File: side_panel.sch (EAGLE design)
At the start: 47 parts

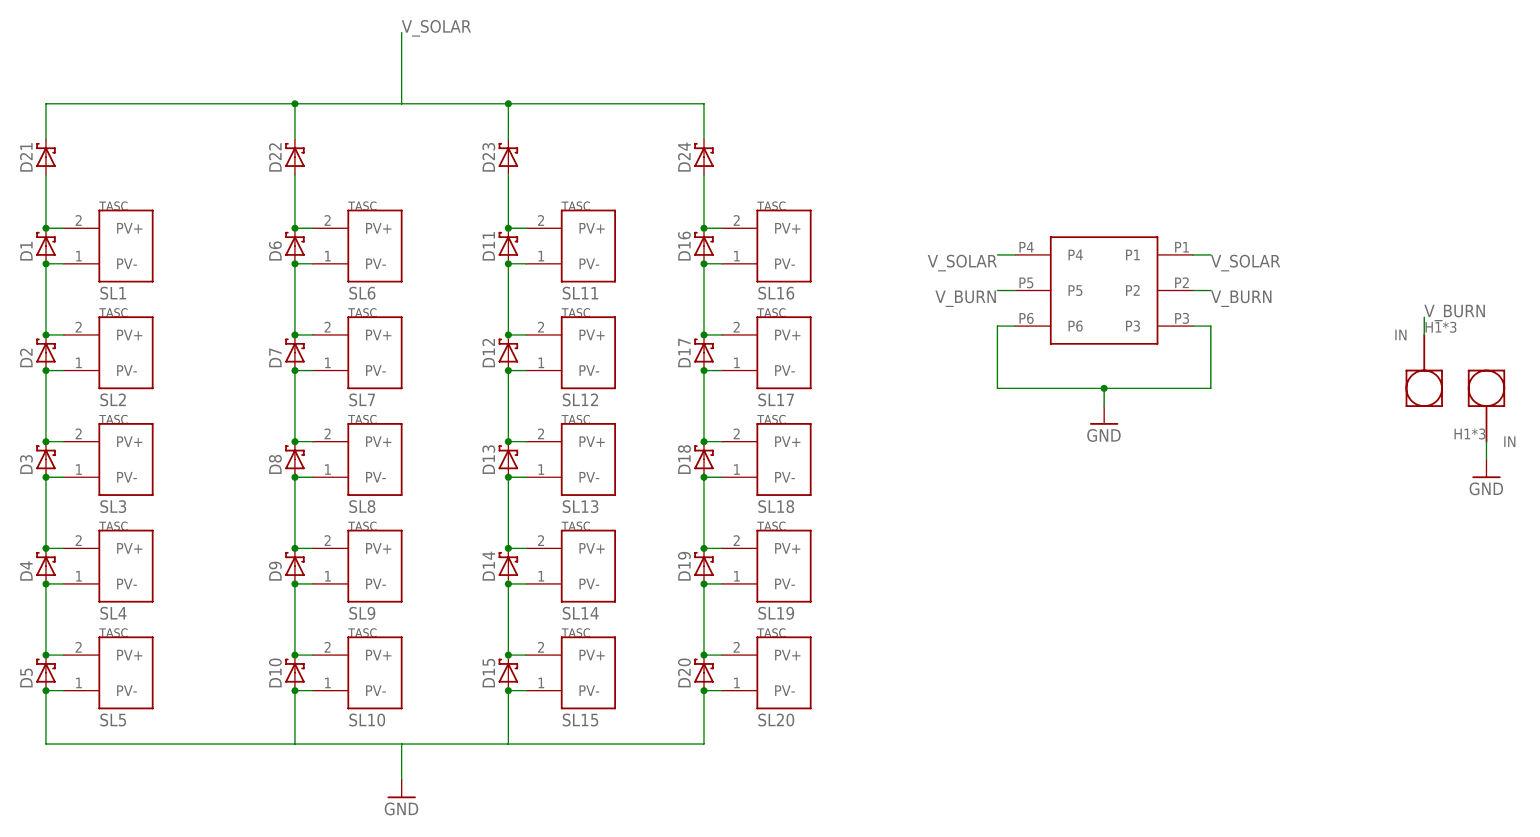
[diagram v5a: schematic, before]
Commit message: Beginning of new solar panel layout
Changing to pairs of TASC cells to accommodate irregularities in
dimensions
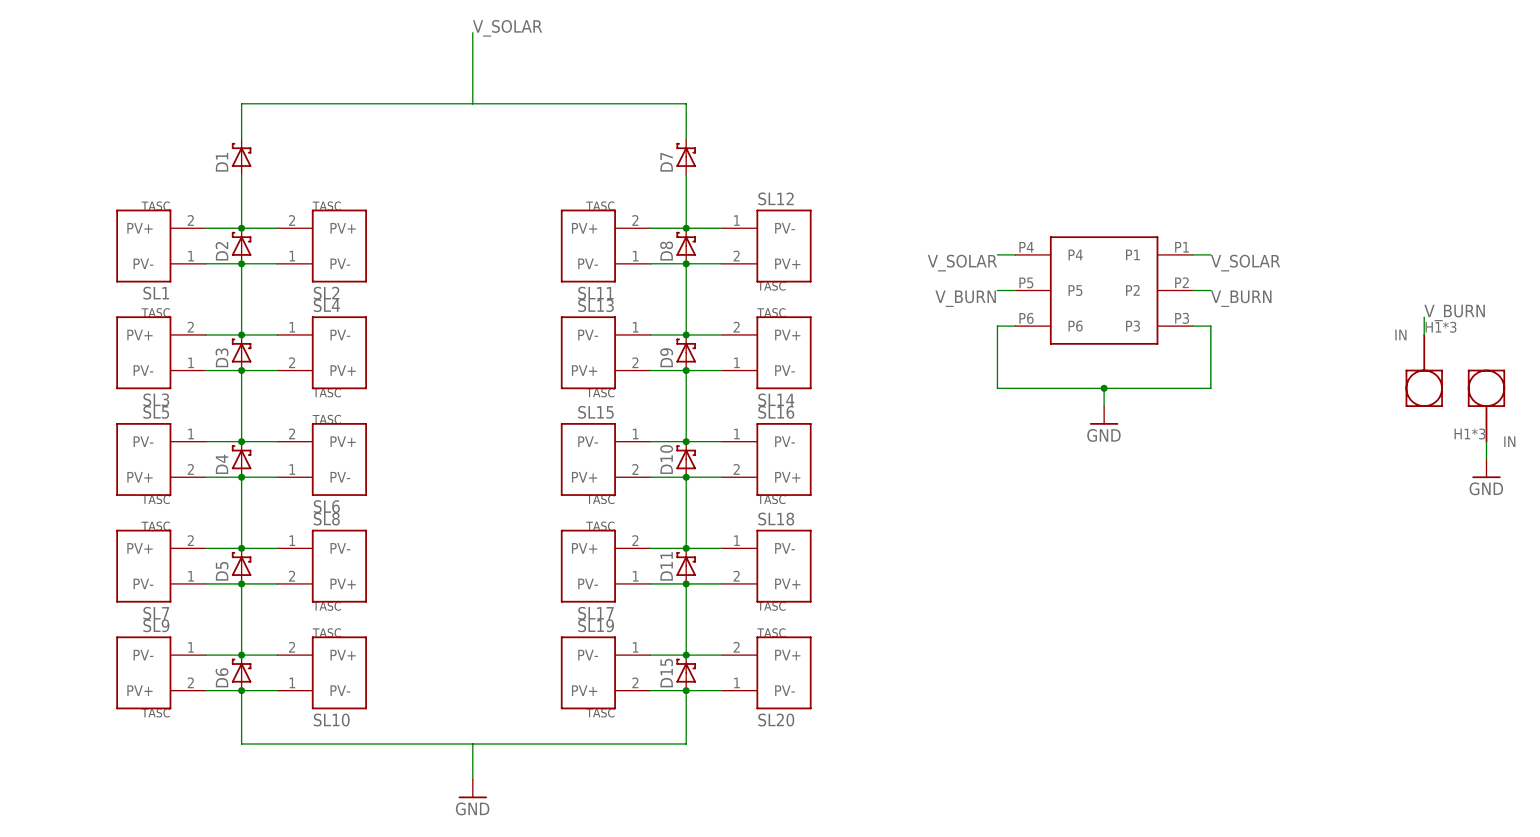
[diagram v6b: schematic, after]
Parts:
- removed D12, D13, D14, D16, D17, D18, D19, D20, D21, D22, D23, D24: SB_DIODE, phonesat:SB_DIODE
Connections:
- removed net N$1: D11.POS, D12.NEG, SL11.PV-, SL12.PV+
- removed net N$11: D10.POS, SL10.PV-
- removed net N$31: D8.POS, D9.NEG, SL8.PV-, SL9.PV+
- removed net N$33: D7.POS, D8.NEG, SL7.PV-, SL8.PV+
- removed net N$35: D10.NEG, D9.POS, SL10.PV+, SL9.PV-
- removed net N$36: D13.POS, D14.NEG, SL13.PV-, SL14.PV+
- removed net N$41: D14.POS, D15.NEG, SL14.PV-, SL15.PV+
- removed net N$5: D11.NEG, D23.POS, SL11.PV+
- removed net N$69: D22.POS, D6.NEG, SL6.PV+
- removed net N$7: D12.POS, D13.NEG, SL12.PV-, SL13.PV+
- removed net N$70: D6.POS, D7.NEG, SL6.PV-, SL7.PV+
- net GND: now also D6.POS, SL10.PV-, SL19.PV+, SL9.PV+; no longer D20.POS, D5.POS, SL15.PV-, SL5.PV-
- net N$2: now also D8.POS, D9.NEG, SL11.PV-, SL12.PV+, SL13.PV-, SL14.PV+; no longer D16.POS, D17.NEG, SL16.PV-, SL17.PV+
- net N$3: now also D10.NEG, D9.POS, SL13.PV+, SL14.PV-, SL15.PV-, SL16.PV-; no longer D17.POS, D18.NEG, SL17.PV-, SL18.PV+
- net N$37: now also D3.POS, D4.NEG, SL3.PV-, SL4.PV+, SL5.PV-, SL6.PV+; no longer D2.POS, D3.NEG, SL2.PV-, SL3.PV+
- net N$39: now also D4.POS, D5.NEG, SL5.PV+, SL6.PV-, SL7.PV+, SL8.PV-; no longer D3.POS, D4.NEG, SL3.PV-, SL4.PV+
- net N$4: now also D10.POS, D11.NEG, SL15.PV+, SL16.PV+, SL17.PV+; no longer D18.POS, D19.NEG, SL19.PV+
- net N$45: now also D2.POS, D3.NEG, SL2.PV-, SL3.PV+, SL4.PV-; no longer D1.POS, D2.NEG, SL2.PV+
- net N$50: now also D5.POS, D6.NEG, SL10.PV+, SL7.PV-, SL8.PV+, SL9.PV-; no longer D4.POS, D5.NEG, SL4.PV-, SL5.PV+
- net N$6: now also D11.POS, D15.NEG, SL17.PV-, SL18.PV+; no longer D19.POS, D20.NEG
- net N$8: now also D7.POS, D8.NEG, SL11.PV+, SL12.PV-; no longer D16.NEG, D24.POS, SL16.PV+
- net N$9: now also D1.POS, D2.NEG, SL2.PV+; no longer D1.NEG, D21.POS
- net V_SOLAR: now also D1.NEG, D7.NEG; no longer D21.NEG, D22.NEG, D23.NEG, D24.NEG
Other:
- moved on the sheet: D1, D10, D11, D15, D2, D3, D4, D5, D6, D7, D8, D9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

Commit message: Fixed some schematic + layout issues on solar panel
This reverts commit 959c03423f2cbd105642679eef46985d8f87b8b7.

Conflicts:
	side_panel.brd
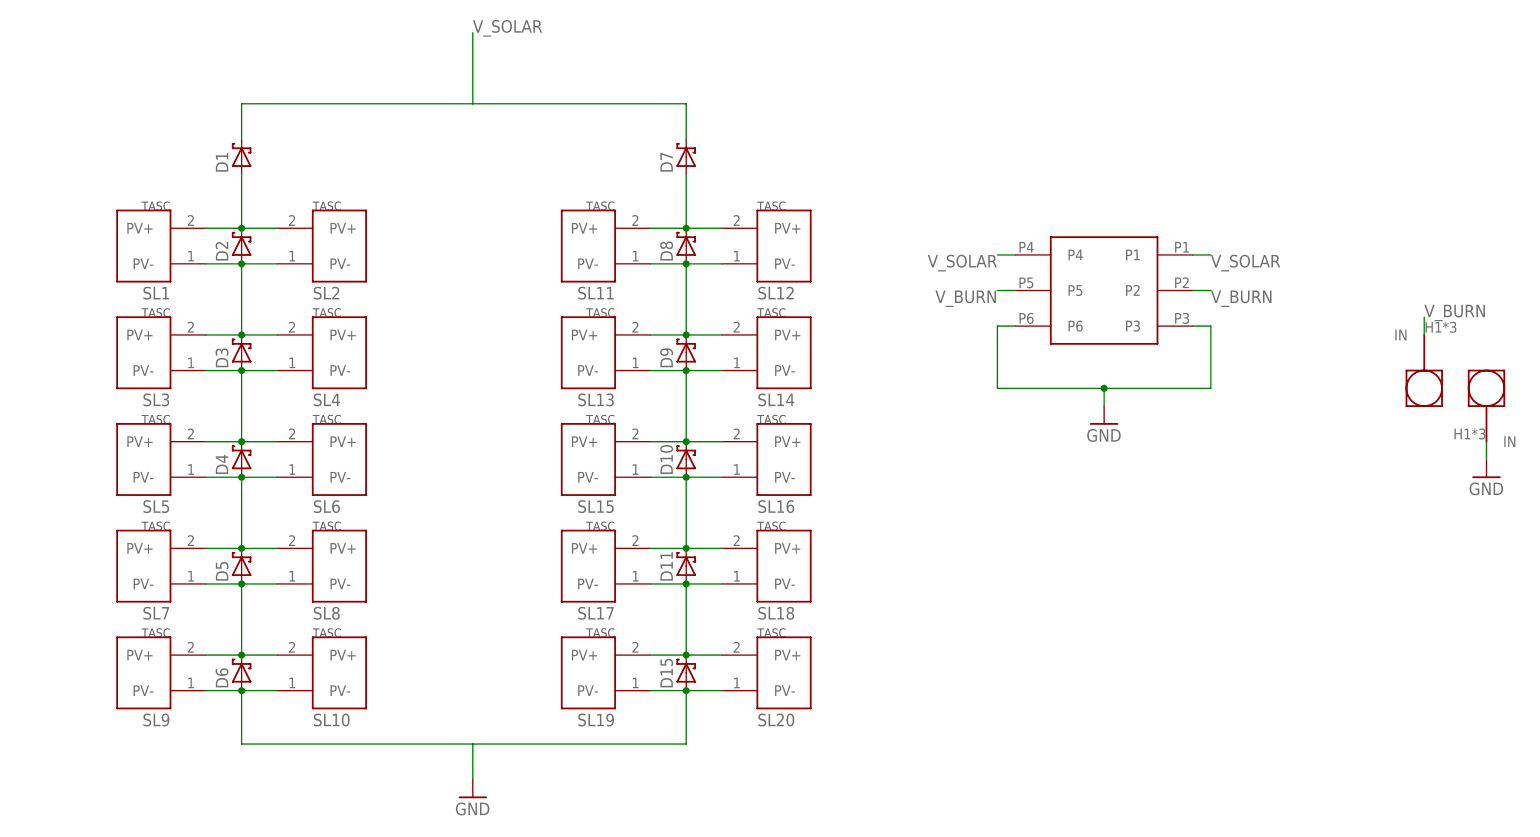
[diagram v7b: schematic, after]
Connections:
- net GND: now also SL19.PV-, SL9.PV-; no longer SL19.PV+, SL9.PV+
- net N$2: now also SL12.PV-, SL13.PV+; no longer SL12.PV+, SL13.PV-
- net N$3: now also SL13.PV-, SL15.PV+, SL16.PV+; no longer SL13.PV+, SL15.PV-, SL16.PV-
- net N$37: now also SL4.PV-, SL5.PV+; no longer SL4.PV+, SL5.PV-
- net N$39: now also SL5.PV-, SL8.PV+; no longer SL5.PV+, SL8.PV-
- net N$4: now also SL15.PV-, SL16.PV-, SL18.PV+; no longer SL15.PV+, SL16.PV+, SL18.PV-
- net N$45: now also SL4.PV+; no longer SL4.PV-
- net N$50: now also SL8.PV-, SL9.PV+; no longer SL8.PV+, SL9.PV-
- net N$6: now also SL18.PV-, SL19.PV+; no longer SL18.PV+, SL19.PV-
- net N$8: now also SL12.PV+; no longer SL12.PV-
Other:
- moved on the sheet: SL12, SL13, SL15, SL16, SL18, SL19, SL4, SL5, SL8, SL9

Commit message: Finished solar panel layout
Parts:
- renumbered D15 to D12
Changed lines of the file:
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@@
 <part name="D10" library="phonesat" deviceset="SB_DIODE" device=""/>
 <part name="D11" library="phonesat" deviceset="SB_DIODE" device=""/>
-<part name="D15" library="phonesat" deviceset="SB_DIODE" device=""/>
+<part name="D12" library="phonesat" deviceset="SB_DIODE" device=""/>
 <part name="D7" library="phonesat" deviceset="SB_DIODE" device=""/>
 <part name="U$1" library="G125-FV20605L0P" deviceset="G125-FV20605L0P" device=""/>
@@
 <attribute name="NAME" x="79.375" y="20.574" size="1.778" layer="95" rot="R90"/>
 </instance>
-<instance part="D15" gate="G$1" x="81.28" y="7.62" smashed="yes" rot="R90">
+<instance part="D12" gate="G$1" x="81.28" y="7.62" smashed="yes" rot="R90">
 <attribute name="NAME" x="79.375" y="5.334" size="1.778" layer="95" rot="R90"/>
 </instance>
@@
 <pinref part="D6" gate="G$1" pin="POS"/>
 <wire x1="81.28" y1="5.08" x2="81.28" y2="-2.54" width="0.1524" layer="91"/>
-<pinref part="D15" gate="G$1" pin="POS"/>
+<pinref part="D12" gate="G$1" pin="POS"/>
 <wire x1="50.8" y1="-2.54" x2="81.28" y2="-2.54" width="0.1524" layer="91"/>
 <pinref part="GND1" gate="1" pin="GND"/>
@@
 <wire x1="81.28" y1="20.32" x2="81.28" y2="10.16" width="0.1524" layer="91"/>
 <pinref part="D11" gate="G$1" pin="POS"/>
-<pinref part="D15" gate="G$1" pin="NEG"/>
+<pinref part="D12" gate="G$1" pin="NEG"/>
 <pinref part="SL20" gate="G$1" pin="PV+"/>
 <wire x1="86.36" y1="10.16" x2="81.28" y2="10.16" width="0.1524" layer="91"/>
